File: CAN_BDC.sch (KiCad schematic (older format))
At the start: 23 parts, among them P1 CONN_01X05, P2 CONN_01X02, P3 CONN_01X02, P4 CONN_01X04, P5 CONN_01X02, U1 STM32F042C6Ux, U2 PSD2CAN, U3 SN65HVD232D, U4 drv8850, U5 MCP1700T-3302E/TT

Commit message: Outline update
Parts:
- removed P4: CONN_01X04, usb_ccb_custom:Pin_Header_Angled_1x04m, symbol CONN_01X04
- added P? (x2): CONN_01X02, Pin_Headers:Pin_Header_Straight_1x02, symbol CONN_01X02
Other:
- note added: "GND\nSWDIO\nSWCLK\nNRST\nVTRG"
- note removed: "SWDIO\nGND\nSWCLK\nNRST\nVTRG"
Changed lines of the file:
@@
 $EndComp
 Text Notes 700  1800 0    60   ~ 0
-SWDIO\nGND\nSWCLK\nNRST\nVTRG
-$Comp
-L GND #PWR02
-U 1 1 57056C83
-P 1700 1450
-F 0 "#PWR02" H 1700 1200 50  0001 C CNN
-F 1 "GND" V 1708 1322 50  0000 R CNN
-F 2 "" H 1700 1450 50  0000 C CNN
-F 3 "" H 1700 1450 50  0000 C CNN
-	1    1700 1450
-	0    -1   -1   0
-$EndComp
-$Comp
-L +3.3V #PWR03
+GND\nSWDIO\nSWCLK\nNRST\nVTRG
+$Comp
+L +3.3V #PWR02
 U 1 1 5706E500
 P 2050 1050
-F 0 "#PWR03" H 2050 900 50  0001 C CNN
+F 0 "#PWR02" H 2050 900 50  0001 C CNN
 F 1 "+3.3V" H 2068 1223 50  0000 C CNN
 F 2 "" H 2050 1050 50  0000 C CNN
@@
 $EndComp
 $Comp
-L +3.3V #PWR04
+L +3.3V #PWR03
 U 1 1 5706E57B
 P 5350 850
-F 0 "#PWR04" H 5350 700 50  0001 C CNN
+F 0 "#PWR03" H 5350 700 50  0001 C CNN
 F 1 "+3.3V" H 5368 1023 50  0000 C CNN
 F 2 "" H 5350 850 50  0000 C CNN
@@
 $EndComp
 $Comp
-L GND #PWR05
+L GND #PWR04
 U 1 1 5706EDB2
 P 8950 1150
-F 0 "#PWR05" H 8950 900 50  0001 C CNN
+F 0 "#PWR04" H 8950 900 50  0001 C CNN
 F 1 "GND" H 8958 977 50  0000 C CNN
 F 2 "" H 8950 1150 50  0000 C CNN
@@
 $EndComp
 $Comp
-L GND #PWR06
+L GND #PWR05
 U 1 1 5706EDDA
 P 9350 1150
-F 0 "#PWR06" H 9350 900 50  0001 C CNN
+F 0 "#PWR05" H 9350 900 50  0001 C CNN
 F 1 "GND" H 9358 977 50  0000 C CNN
 F 2 "" H 9350 1150 50  0000 C CNN
@@
 $EndComp
 $Comp
-L +3.3V #PWR07
+L +3.3V #PWR06
 U 1 1 5706EE52
 P 9350 850
-F 0 "#PWR07" H 9350 700 50  0001 C CNN
+F 0 "#PWR06" H 9350 700 50  0001 C CNN
 F 1 "+3.3V" H 9368 1023 50  0000 C CNN
 F 2 "" H 9350 850 50  0000 C CNN
@@
 $EndComp
 $Comp
-L +3.3V #PWR08
+L +3.3V #PWR07
 U 1 1 5706EEDE
 P 8950 850
-F 0 "#PWR08" H 8950 700 50  0001 C CNN
+F 0 "#PWR07" H 8950 700 50  0001 C CNN
 F 1 "+3.3V" H 8968 1023 50  0000 C CNN
 F 2 "" H 8950 850 50  0000 C CNN
@@
 $EndComp
 $Comp
-L +3.3V #PWR09
+L +3.3V #PWR08
 U 1 1 5708A6C5
 P 10800 5050
-F 0 "#PWR09" H 10800 4900 50  0001 C CNN
+F 0 "#PWR08" H 10800 4900 50  0001 C CNN
 F 1 "+3.3V" H 10818 5223 50  0000 C CNN
 F 2 "" H 10800 5050 50  0000 C CNN
@@
 $EndComp
 $Comp
-L GND #PWR010
+L GND #PWR09
 U 1 1 5708A9FB
 P 10800 5350
-F 0 "#PWR010" H 10800 5100 50  0001 C CNN
+F 0 "#PWR09" H 10800 5100 50  0001 C CNN
 F 1 "GND" V 10808 5222 50  0000 R CNN
 F 2 "" H 10800 5350 50  0000 C CNN
@@
 $EndComp
 $Comp
-L GND #PWR011
+L GND #PWR010
 U 1 1 5708B621
 P 10500 5350
-F 0 "#PWR011" H 10500 5100 50  0001 C CNN
+F 0 "#PWR010" H 10500 5100 50  0001 C CNN
 F 1 "GND" V 10508 5222 50  0000 R CNN
 F 2 "" H 10500 5350 50  0000 C CNN
@@
 $EndComp
 $Comp
-L GND #PWR012
+L GND #PWR011
 U 1 1 5708BDA5
 P 10250 5350
-F 0 "#PWR012" H 10250 5100 50  0001 C CNN
+F 0 "#PWR011" H 10250 5100 50  0001 C CNN
 F 1 "GND" V 10258 5222 50  0000 R CNN
 F 2 "" H 10250 5350 50  0000 C CNN
@@
 $EndComp
 $Comp
-L GND #PWR013
+L GND #PWR012
 U 1 1 5708D67B
 P 7500 6050
-F 0 "#PWR013" H 7500 5800 50  0001 C CNN
+F 0 "#PWR012" H 7500 5800 50  0001 C CNN
 F 1 "GND" V 7508 5922 50  0000 R CNN
 F 2 "" H 7500 6050 50  0000 C CNN
@@
 Text GLabel 8650 3950 2    60   Input ~ 0
 SW_CLK
-Text GLabel 1550 1350 2    60   Input ~ 0
+Text GLabel 1550 1450 2    60   Input ~ 0
 SW_DIO
 Text GLabel 8650 3850 2    60   Input ~ 0
 SW_DIO
 $Comp
-L GND #PWR014
+L GND #PWR013
 U 1 1 571ACD79
 P 9350 2850
-F 0 "#PWR014" H 9350 2600 50  0001 C CNN
+F 0 "#PWR013" H 9350 2600 50  0001 C CNN
 F 1 "GND" H 9450 2700 50  0000 C CNN
 F 2 "" H 9350 2850 50  0000 C CNN
@@
 	-1   0    0    1
 $EndComp
-$Comp
-L CONN_01X04 P4
-U 1 1 571E76C6
-P 9700 3000
-F 0 "P4" H 9777 2992 50  0000 L CNN
-F 1 "CONN_01X04" H 9778 2947 50  0001 L CNN
-F 2 "usb_ccb_custom:Pin_Header_Angled_1x04m" H 9777 2947 50  0001 L CNN
-F 3 "" H 9700 3000 50  0000 C CNN
-	1    9700 3000
-	1    0    0    -1
-$EndComp
 Text Label 8950 3050 0    60   ~ 0
 USART_TX
@@
 USART_RX
 $Comp
-L CONN_01X05 P1
-U 1 1 57800591
-P 1050 1550
-F 0 "P1" H 969 1211 50  0000 C CNN
-F 1 "CONN_01X05" H 969 1210 50  0001 C CNN
-F 2 "usb_ccb_custom:swd_smd_conn5" H 969 1211 50  0001 C CNN
-F 3 "" H 1050 1550 50  0000 C CNN
-	1    1050 1550
-	-1   0    0    1
-$EndComp
-$Comp
-L +3.3V #PWR015
+L +3.3V #PWR014
 U 1 1 57800AA2
 P 1250 1750
-F 0 "#PWR015" H 1250 1600 50  0001 C CNN
+F 0 "#PWR014" H 1250 1600 50  0001 C CNN
 F 1 "+3.3V" H 1268 1923 50  0000 C CNN
 F 2 "" H 1250 1750 50  0000 C CNN
@@
 ucandevices.pl CBDC 1.0\n
 $Comp
-L +5V #PWR016
+L +5V #PWR015
 U 1 1 57F6DC22
 P 4050 5050
-F 0 "#PWR016" H 4050 4900 50  0001 C CNN
+F 0 "#PWR015" H 4050 4900 50  0001 C CNN
 F 1 "+5V" H 4068 5223 50  0000 C CNN
 F 2 "" H 4050 5050 50  0000 C CNN
@@
 $EndComp
 $Comp
-L +3.3V #PWR017
+L +3.3V #PWR016
 U 1 1 57F6DF04
 P 9500 2850
-F 0 "#PWR017" H 9500 2700 50  0001 C CNN
+F 0 "#PWR016" H 9500 2700 50  0001 C CNN
 F 1 "+3.3V" H 9518 3023 50  0000 C CNN
 F 2 "" H 9500 2850 50  0000 C CNN
@@
 $EndComp
 $Comp
-L GND #PWR018
+L GND #PWR017
 U 1 1 57F6DF30
 P 4050 5150
-F 0 "#PWR018" H 4050 4900 50  0001 C CNN
+F 0 "#PWR017" H 4050 4900 50  0001 C CNN
 F 1 "GND" H 4058 4977 50  0000 C CNN
 F 2 "" H 4050 5150 50  0000 C CNN
@@
 $EndComp
 $Comp
-L GNDA #PWR019
+L GNDA #PWR018
 U 1 1 57F8004B
 P 2450 5400
-F 0 "#PWR019" H 2450 5150 50  0001 C CNN
+F 0 "#PWR018" H 2450 5150 50  0001 C CNN
 F 1 "GNDA" H 2458 5227 50  0000 C CNN
 F 2 "" H 2450 5400 50  0000 C CNN
@@
 $EndComp
 $Comp
-L GNDA #PWR020
+L GNDA #PWR019
 U 1 1 57F80189
 P 2300 6900
-F 0 "#PWR020" H 2300 6650 50  0001 C CNN
+F 0 "#PWR019" H 2300 6650 50  0001 C CNN
 F 1 "GNDA" H 2308 6727 50  0000 C CNN
 F 2 "" H 2300 6900 50  0000 C CNN
@@
 $EndComp
 $Comp
-L GNDA #PWR021
+L GNDA #PWR020
 U 1 1 57F8135B
 P 3600 6400
-F 0 "#PWR021" H 3600 6150 50  0001 C CNN
+F 0 "#PWR020" H 3600 6150 50  0001 C CNN
 F 1 "GNDA" H 3700 6250 50  0000 C CNN
 F 2 "" H 3600 6400 50  0000 C CNN
@@
 $EndComp
 $Comp
-L GNDA #PWR022
+L GNDA #PWR021
 U 1 1 57F83C95
 P 1250 6850
-F 0 "#PWR022" H 1250 6600 50  0001 C CNN
+F 0 "#PWR021" H 1250 6600 50  0001 C CNN
 F 1 "GNDA" H 1258 6677 50  0000 C CNN
 F 2 "" H 1250 6850 50  0000 C CNN
@@
 $EndComp
 $Comp
-L +5V #PWR023
+L +5V #PWR022
 U 1 1 57F843CB
 P 4050 6100
-F 0 "#PWR023" H 4050 5950 50  0001 C CNN
+F 0 "#PWR022" H 4050 5950 50  0001 C CNN
 F 1 "+5V" H 4068 6273 50  0000 C CNN
 F 2 "" H 4050 6100 50  0000 C CNN
@@
 $EndComp
 $Comp
-L GND #PWR027
+L GND #PWR023
 U 1 1 57F9604D
 P 5850 5600
-F 0 "#PWR027" H 5850 5350 50  0001 C CNN
+F 0 "#PWR023" H 5850 5350 50  0001 C CNN
 F 1 "GND" H 5858 5427 50  0000 C CNN
 F 2 "" H 5850 5600 50  0000 C CNN
@@
 $EndComp
 $Comp
-L +5V #PWR028
+L +5V #PWR024
 U 1 1 57F969C6
 P 4950 5300
-F 0 "#PWR028" H 4950 5150 50  0001 C CNN
+F 0 "#PWR024" H 4950 5150 50  0001 C CNN
 F 1 "+5V" H 4968 5473 50  0000 C CNN
 F 2 "" H 4950 5300 50  0000 C CNN
@@
 $EndComp
 $Comp
-L +3.3V #PWR029
+L +3.3V #PWR025
 U 1 1 57F96BE3
 P 5850 5300
-F 0 "#PWR029" H 5850 5150 50  0001 C CNN
+F 0 "#PWR025" H 5850 5150 50  0001 C CNN
 F 1 "+3.3V" H 5950 5450 50  0000 C CNN
 F 2 "" H 5850 5300 50  0000 C CNN
@@
 BMF1
 $Comp
-L GNDA #PWR030
+L GNDA #PWR026
 U 1 1 57F9B056
 P 4950 5600
-F 0 "#PWR030" H 4950 5350 50  0001 C CNN
+F 0 "#PWR026" H 4950 5350 50  0001 C CNN
 F 1 "GNDA" H 4958 5427 50  0000 C CNN
 F 2 "" H 4950 5600 50  0000 C CNN
@@
 $EndComp
 $Comp
-L GNDA #PWR031
+L GNDA #PWR027
 U 1 1 57F820AC
 P 3400 6400
-F 0 "#PWR031" H 3400 6150 50  0001 C CNN
+F 0 "#PWR027" H 3400 6150 50  0001 C CNN
 F 1 "GNDA" H 3450 6250 50  0000 C CNN
 F 2 "" H 3400 6400 50  0000 C CNN
@@
 Wire Wire Line
 	2050 1350 2450 1350
-Wire Wire Line
-	1250 1450 1700 1450
 Connection ~ 10500 5050
 Connection ~ 10800 5050
@@
 Wire Wire Line
 	1250 1550 1550 1550
-Wire Wire Line
-	1550 1350 1250 1350
 Wire Wire Line
 	8850 3050 8850 2750
@@
 $EndComp
 $Comp
-L GNDA #PWR032
+L GNDA #PWR028
 U 1 1 57FC2643
 P 3850 5600
-F 0 "#PWR032" H 3850 5350 50  0001 C CNN
+F 0 "#PWR028" H 3850 5350 50  0001 C CNN
 F 1 "GNDA" H 3950 5450 50  0000 C CNN
 F 2 "" H 3850 5600 50  0000 C CNN
@@
 $EndComp
 $Comp
-L GND #PWR033
+L GND #PWR029
 U 1 1 57FC269C
 P 3650 5600
-F 0 "#PWR033" H 3650 5350 50  0001 C CNN
+F 0 "#PWR029" H 3650 5350 50  0001 C CNN
 F 1 "GND" H 3658 5427 50  0000 C CNN
 F 2 "" H 3650 5600 50  0000 C CNN
@@
 Text GLabel 1550 6400 0    60   Input ~ 0
 nSLEEP
+Wire Wire Line
+	1250 1450 1550 1450
+$Comp
+L CONN_01X05 P1
+U 1 1 57800591
+P 1050 1550
+F 0 "P1" H 969 1211 50  0000 C CNN
+F 1 "CONN_01X05" H 969 1210 50  0001 C CNN
+F 2 "usb_ccb_custom:swd_smd_conn5" H 969 1211 50  0001 C CNN
+F 3 "" H 1050 1550 50  0000 C CNN
+	1    1050 1550
+	-1   0    0    1
+$EndComp
+Wire Wire Line
+	1550 1350 1250 1350
+$Comp
+L GND #PWR02
+U 1 1 57056C83
+P 1550 1350
+F 0 "#PWR02" H 1550 1100 50  0001 C CNN
+F 1 "GND" V 1558 1222 50  0000 R CNN
+F 2 "" H 1550 1350 50  0000 C CNN
+F 3 "" H 1550 1350 50  0000 C CNN
+	1    1550 1350
+	0    -1   -1   0
+$EndComp
+$Comp
+L CONN_01X02 P?
+U 1 1 57FD66CE
+P 9700 2900
+F 0 "P?" H 9850 3000 50  0000 C CNN
+F 1 "CONN_01X02" V 9574 2756 50  0001 R CNN
+F 2 "Pin_Headers:Pin_Header_Straight_1x02" H 9700 2900 50  0001 C CNN
+F 3 "" H 9700 2900 50  0000 C CNN
+	1    9700 2900
+	1    0    0    -1
+$EndComp
+$Comp
+L CONN_01X02 P?
+U 1 1 57FD69A3
+P 9700 3100
+F 0 "P?" H 9850 3200 50  0000 C CNN
+F 1 "CONN_01X02" V 9574 2956 50  0001 R CNN
+F 2 "Pin_Headers:Pin_Header_Straight_1x02" H 9700 3100 50  0001 C CNN
+F 3 "" H 9700 3100 50  0000 C CNN
+	1    9700 3100
+	1    0    0    -1
+$EndComp
 $EndSCHEMATC

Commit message: Connector update
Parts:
- gave numbers to parts that had none: 2
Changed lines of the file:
@@
 	1550 1350 1250 1350
 $Comp
-L GND #PWR02
+L GND #PWR030
 U 1 1 57056C83
 P 1550 1350
-F 0 "#PWR02" H 1550 1100 50  0001 C CNN
+F 0 "#PWR030" H 1550 1100 50  0001 C CNN
 F 1 "GND" V 1558 1222 50  0000 R CNN
 F 2 "" H 1550 1350 50  0000 C CNN
@@
 $EndComp
 $Comp
-L CONN_01X02 P?
+L CONN_01X02 P4
 U 1 1 57FD66CE
 P 9700 2900
-F 0 "P?" H 9850 3000 50  0000 C CNN
+F 0 "P4" H 9850 3000 50  0000 C CNN
 F 1 "CONN_01X02" V 9574 2756 50  0001 R CNN
 F 2 "Pin_Headers:Pin_Header_Straight_1x02" H 9700 2900 50  0001 C CNN
@@
 $EndComp
 $Comp
-L CONN_01X02 P?
+L CONN_01X02 P6
 U 1 1 57FD69A3
 P 9700 3100
-F 0 "P?" H 9850 3200 50  0000 C CNN
+F 0 "P6" H 9850 3200 50  0000 C CNN
 F 1 "CONN_01X02" V 9574 2956 50  0001 R CNN
 F 2 "Pin_Headers:Pin_Header_Straight_1x02" H 9700 3100 50  0001 C CNN

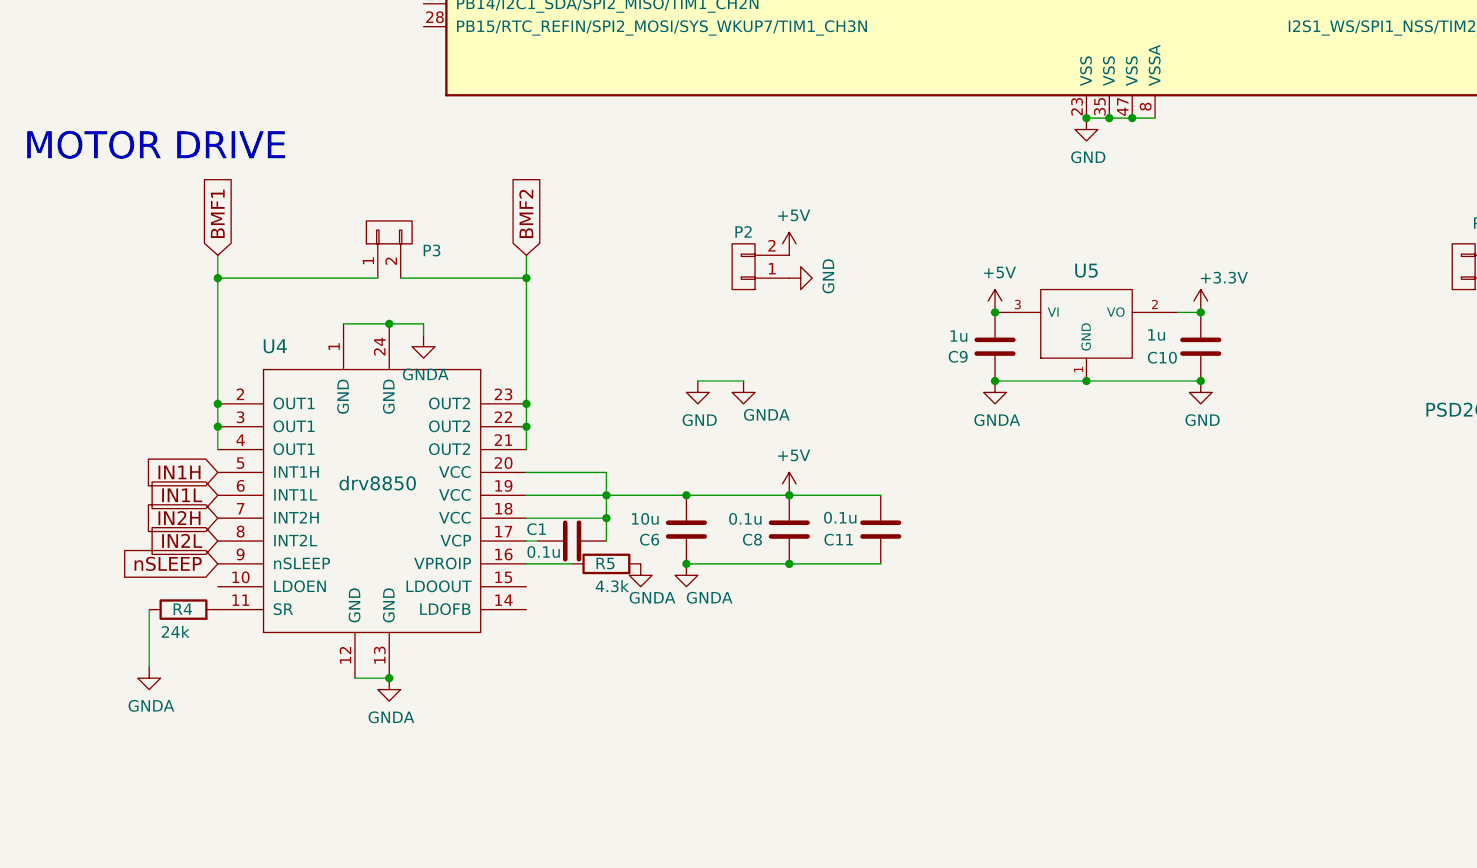
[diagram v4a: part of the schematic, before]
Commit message: DRV8834 Addition
DRV8834 Addition
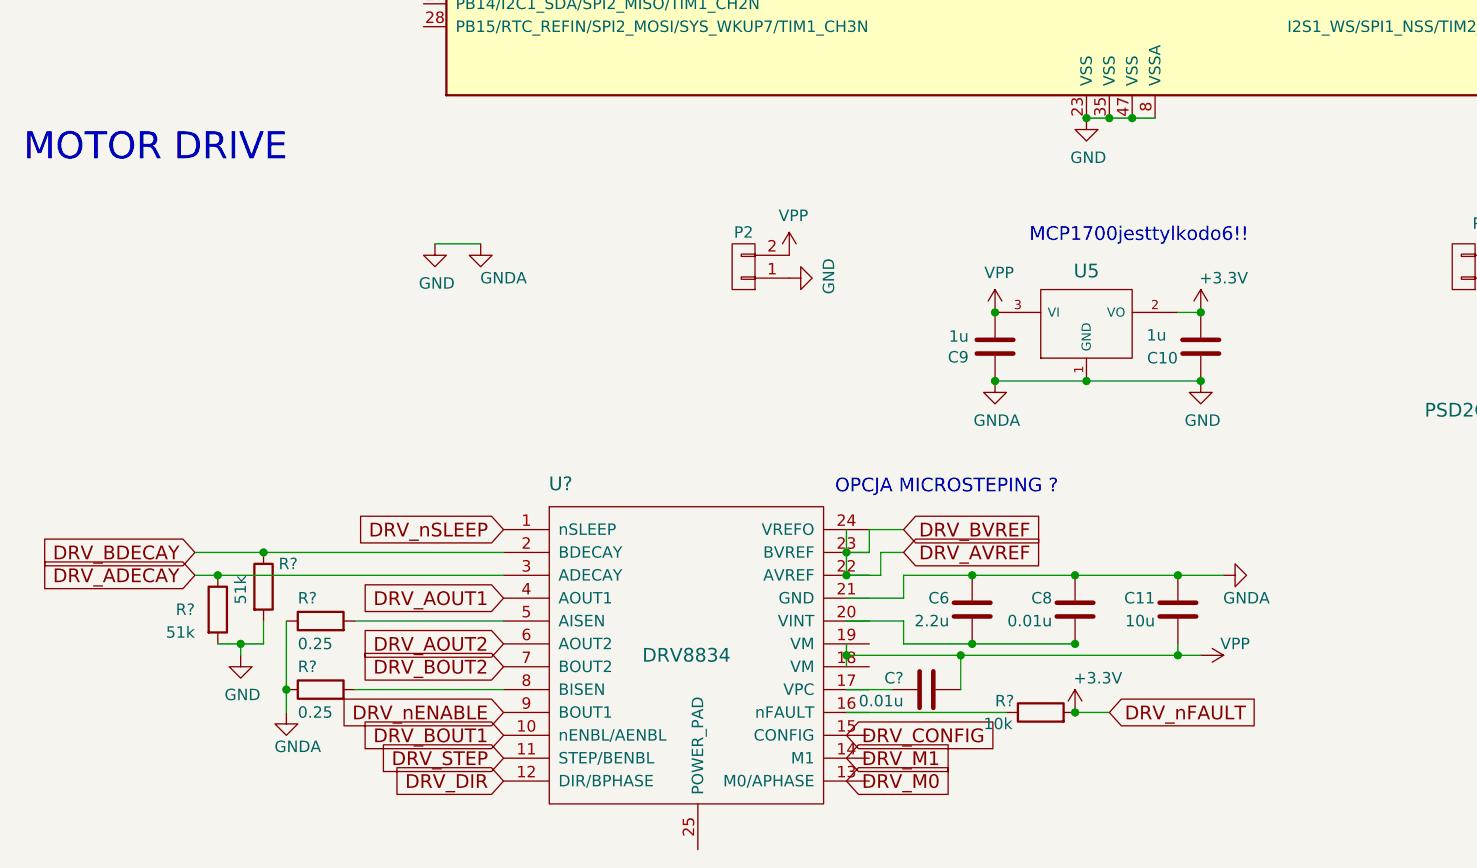
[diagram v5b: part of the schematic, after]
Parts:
- removed C1: 0.1u, Capacitors_SMD:C_0402, symbol C
- removed P3: CONN_01X02, Pin_Headers:Pin_Header_Straight_1x02, symbol CONN_01X02
- removed R4: 24k, Resistors_SMD:R_0402, symbol R
- removed R5: 4.3k, Resistors_SMD:R_0402, symbol R
- removed U4: drv8850, usb_ccb_custom:drv8850, symbol drv8850
- added C?: 0.01u, Capacitors_SMD:C_0402, symbol C
- added R?: 10k, Resistors_SMD:R_0402, symbol R
- added R? (x2): 0.25, Resistors_SMD:R_0402, symbol R
- added R? (x2): 51k, Resistors_SMD:R_0402, symbol R
- added U?: DRV8834, usb_ccb_custom:HTSSOP, symbol DRV8834
- C11: value 0.1u -> 10u
- C6: value 10u -> 2.2u
- C8: value 0.1u -> 0.01u
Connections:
- net labels added: DRV_ADECAY, DRV_AOUT1, DRV_AOUT2, DRV_AVREF, DRV_BDECAY, DRV_BOUT1, DRV_BOUT2, DRV_BVREF, DRV_CONFIG, DRV_DIR, DRV_M0, DRV_M1, DRV_STEP, DRV_nENABLE, DRV_nFAULT, DRV_nSLEEP, VPP
- net labels removed: +5V, BMF1, BMF2, IN1H, IN1L, IN2H, IN2L, nSLEEP
- wire segments 41 -> 54
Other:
- note added: "MCP1700jesttylkodo6!!"
- note added: "OPCJA MICROSTEPING ?\n"
- moved on the sheet: C11, C6, C8
